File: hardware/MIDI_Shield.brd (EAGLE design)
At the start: 59.7 x 53.3 mm, 24 parts, among them U1 ARDUINO_SHIELDLABEL

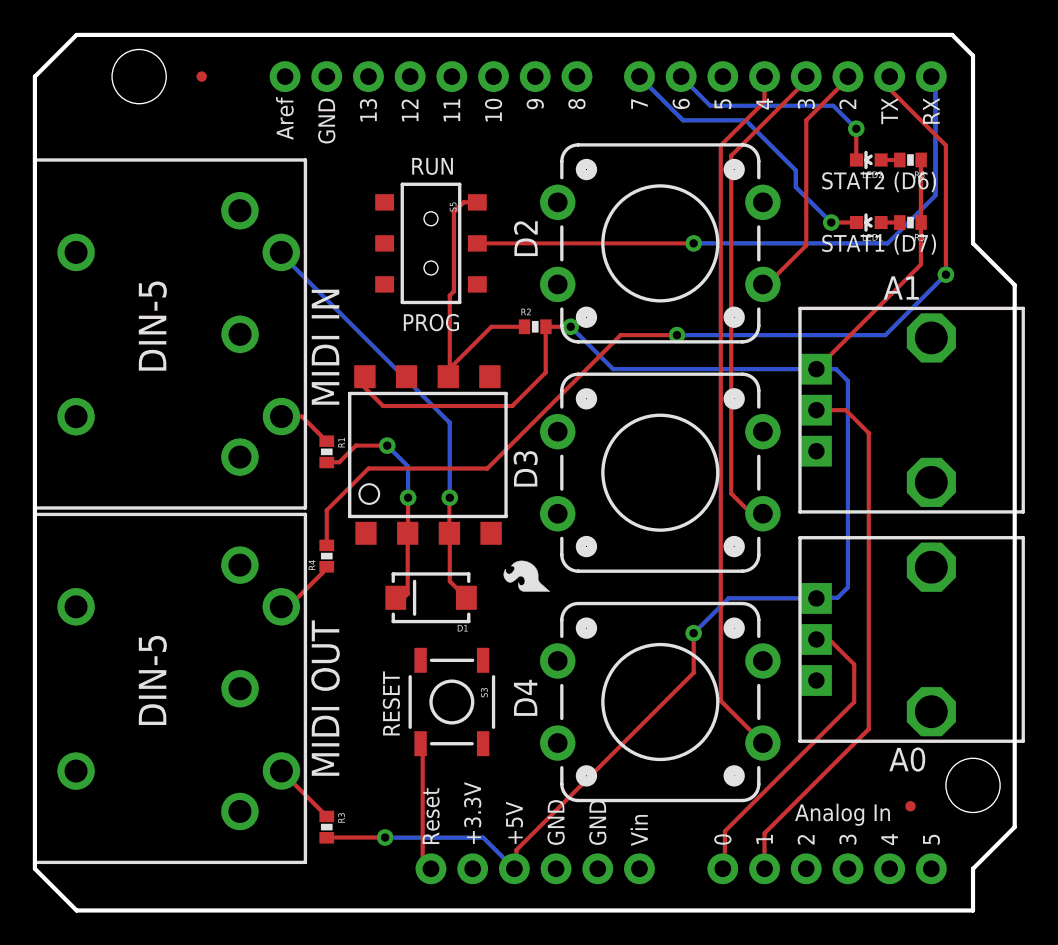
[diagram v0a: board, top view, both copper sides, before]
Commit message: Added pin 2 ground, 0603, oshw, v#, trace/sch rework
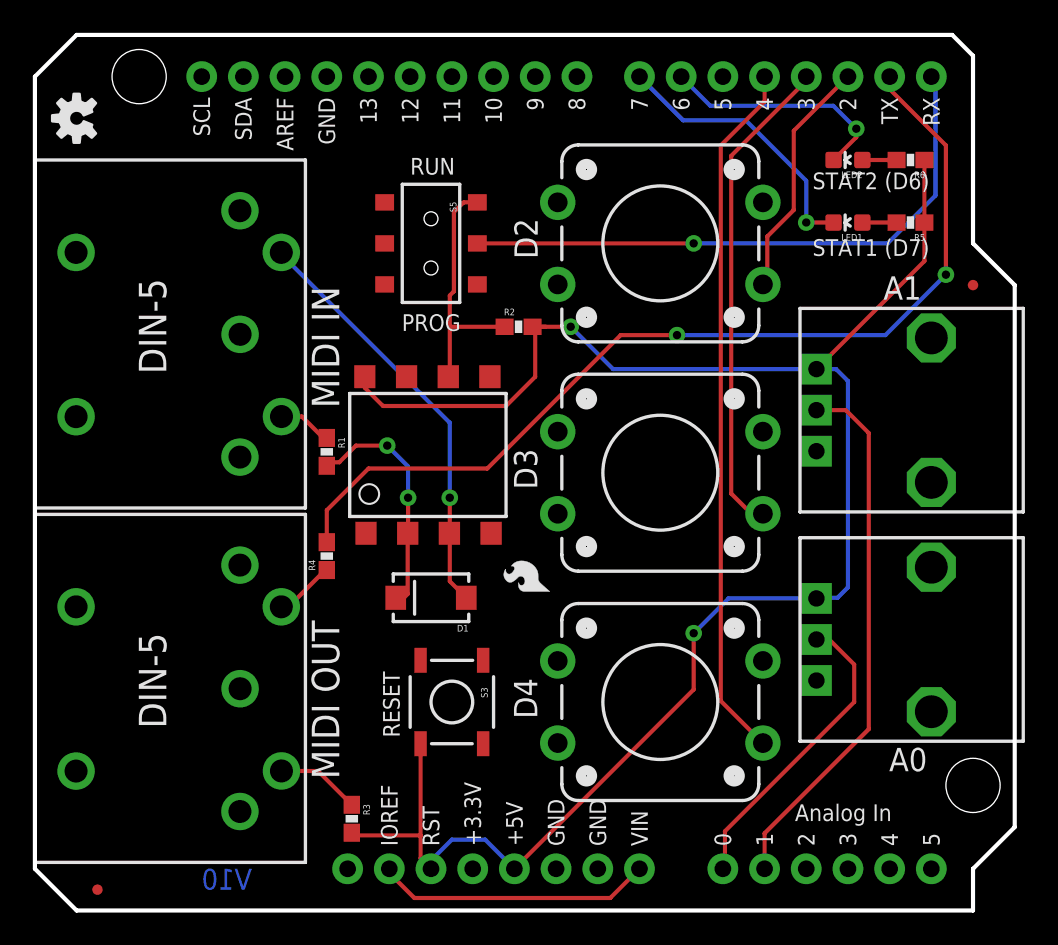
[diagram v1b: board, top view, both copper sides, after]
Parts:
- removed U1: ARDUINO_SHIELDLABEL, SparkFun:DUEMILANOVE_SHIELD
- added U$1: ARDUINO_R3_SHIELD, SparkFun-Boards:UNO_R3_SHIELD
- added U$2, U$3: (no value), SparkFun-Electromechanical:STAND-OFF
- added U$4: (no value), SparkFun-Aesthetics:OSHW-LOGO-S
- LED1, LED2: device SparkFun:LED-0603 -> SparkFun-LED:LED-0603
- R1, R2, R3, R4, R5, R6: device SparkFun:0402-RES -> SparkFun-Resistors:0603-RES
- moved JP2 49.8 mm to (3.81, 1.27)
- moved JP1 48.7 mm to (57.1, 38.1)
- moved R3 1.61 mm to (19.3, 5.59)
- moved LED1 1.27 mm to (49.5, 41.9)
- moved LED2 1.27 mm to (49.5, 45.7)
- moved R2 1.02 mm to (29.5, 35.6)
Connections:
- removed net RESET: S3.4, U1.RES
- net 3.3V: now also U$1.3.3V; no longer U1.3.3V
- net A0: now also U$1.A0; no longer U1.A0
- net A1: now also U$1.A1; no longer U1.A1
- net A2: now also U$1.A2; no longer U1.A2
- net A3: now also U$1.A3; no longer U1.A3
- net A4: now also U$1.A4; no longer U1.A4
- net A5: now also U$1.A5; no longer U1.A5
- net AREF: now also U$1.AREF; no longer U1.AREF
- net D10: now also U$1.D10; no longer U1.D10
- net D11: now also U$1.D11; no longer U1.D11
- net D12: now also U$1.D12; no longer U1.D12
- net D13: now also U$1.D13; no longer U1.D13
- net D2: now also U$1.D2; no longer U1.D2
- net D3: now also U$1.D3; no longer U1.D3
- net D4: now also U$1.D4; no longer U1.D4
- net D5: now also U$1.D5; no longer U1.D5
- net D6: now also U$1.D6; no longer U1.D6
- net D7: now also U$1.D7; no longer U1.D7
- net D8: now also U$1.D8; no longer U1.D8
- net D9: now also U$1.D9; no longer U1.D9
- net GND: now also OUT_CON.2, U$1.GND@0, U$1.GND@1, U$1.GND@2; no longer U1.GND@0, U1.GND@1, U1.GND@2
- net RX-I: now also U$1.RX; no longer U1.RX
- net TX: now also U$1.TX; no longer U1.TX
- net VCC: now also S3.4, U$1.5V, U$1.RES; no longer U1.5V
- net VIN: now also U$1.IOREF, U$1.VIN; no longer U1.VIN
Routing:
- net VIN: track 0.00 -> 16.9 mm
- net RESET: track 8.14 -> 0.00 mm
- net VCC: track 105.6 -> 113.3 mm, vias 3 -> 2
- net RX: track 18.9 -> 16.3 mm
- net N$9: track 1.14 -> 2.08 mm
- net N$10: track 1.14 -> 2.08 mm
- net 1235: track 4.27 -> 5.14 mm
- net D6: track 13.9 -> 14.5 mm
- net D7: track 17.5 -> 17.0 mm
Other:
- board text added: "V10"
